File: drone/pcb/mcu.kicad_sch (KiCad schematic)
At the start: 33 parts, among them J1 Conn_01x02_Pin, SW2 SW_Push, U1 TLV1117LV33DCYR, U2 W25Q64JVSSIQ_C179171, U3 STM32H750VBTx, Y1 25 MHz

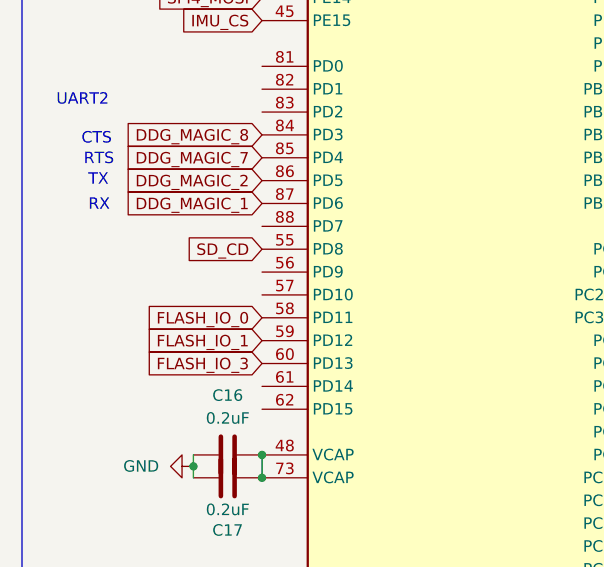
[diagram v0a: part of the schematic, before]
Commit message: [pcb] add JST FPV connector
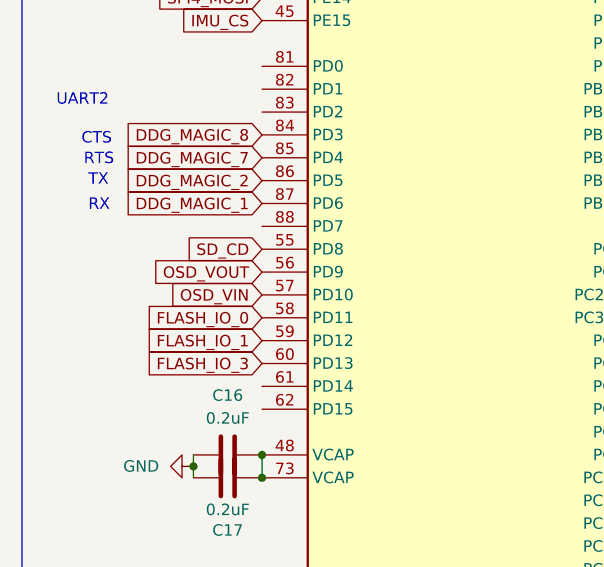
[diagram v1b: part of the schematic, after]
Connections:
- net OSD_VOUT: now reaches U3.56 (PD9)
- net OSD_VIN: now reaches U3.57 (PD10)
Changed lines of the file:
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@@
+		)
+	)
+	(global_label "OSD_VIN"
+		(shape input)
+		(at 41.91 137.16 180)
+		(fields_autoplaced yes)
+		(effects
+			(font
+				(size 1.27 1.27)
+			)
+			(justify right)
+		)
+		(property "Intersheetrefs" "${INTERSHEET_REFS}"
+			(at 31.1233 137.16 0)
+			(effects
+				(font
+					(size 1.27 1.27)
+				)
+				(justify right)
+				(hide yes)
+			)
 		)
 	)
@@
 			(effects
 				(font
+					(size 1.27 1.27)
+				)
+				(justify right)
+				(hide yes)
+			)
+		)
+	)
+	(global_label "OSD_VOUT"
+		(shape input)
+		(at 41.91 134.62 180)
+		(fields_autoplaced yes)
+		(effects
+			(font
+				(size 1.27 1.27)
+			)
+			(justify right)
+		)
+		(property "Intersheetrefs" "${INTERSHEET_REFS}"
+			(at 29.43 134.62 0)
+			(effects
+				(font

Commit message: [bom] change battery and [controller] add button 3d files
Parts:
- J1: footprint Connector_JST:JST_XH_B2B-XH-A_1x02_P2.50mm_Vertical -> Connector_JST:JST_PH_B2B-PH-K_1x02_P2.00mm_Vertical
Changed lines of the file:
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@@
 			)
 		)
-		(property "Footprint" "Connector_JST:JST_XH_B2B-XH-A_1x02_P2.50mm_Vertical"
+		(property "Footprint" "Connector_JST:JST_PH_B2B-PH-K_1x02_P2.00mm_Vertical"
 			(at 200.66 21.59 0)
 			(effects

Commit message: [pcb] update battery connector footprint
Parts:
- J1: footprint Connector_JST:JST_PH_B2B-PH-K_1x02_P2.00mm_Vertical -> Connector_Wire:SolderWire-0.1sqmm_1x02_P3.6mm_D0.4mm_OD1mm
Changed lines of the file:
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@@
 			)
 		)
-		(property "Footprint" "Connector_JST:JST_PH_B2B-PH-K_1x02_P2.00mm_Vertical"
+		(property "Footprint" "Connector_Wire:SolderWire-0.1sqmm_1x02_P3.6mm_D0.4mm_OD1mm"
 			(at 200.66 21.59 0)
 			(effects
